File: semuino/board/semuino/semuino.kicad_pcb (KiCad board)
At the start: 2 copper layers, 95 x 95 mm, 63 parts, among them J1 12V_POWER_IN, J10 POW LED 3, J11 RF ON/OFF, J12 Screen, J13 Earth humidity sensor, J14 Select, J2 Select, J3 12V_POWER_OUT, J4 5V_POWER_IN, J5 RGB 1, J6 RGB 2, J7 RGB 3, J8 POW LED 1, J9 POW LED 2, Q1 2N2222A, Q2 P03P4L-04, Q3 2N2222A, Q4 2N2222A, Q5 2N2222A, Q6 P03P4L-04, Q7 P03P4L-04, Q8 P03P4L-04, U1 RtcArduino, U2 BPC_ESP8266-01_ESP-01, U3 BPC_DHT22, U4 BPC_Alim3_3V

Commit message: Après nettoyage et vérification des règles
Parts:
- removed ? (x3): , 
- moved R14 0.87 mm to (122.2, 58.5)
- moved J6 0.50 mm to (189.0, 111.0)
- moved J7 0.50 mm to (189.0, 100.0)
- moved Q3 0.50 mm to (130.5, 96.5)
- moved J4 0.46 mm to (177.0, 131.0)
- moved J5 0.46 mm to (189.0, 122.0)
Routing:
- net Net-(J6-Pin_2): track 43.0 -> 49.5 mm
- net Net-(Q8-S): track 18.4 -> 20.2 mm
- net SCL: track 119.2 -> 117.5 mm
- net Hum3: track 61.9 -> 60.4 mm
- net CmdP2: track 60.9 -> 59.6 mm
- net CmdP1: track 75.2 -> 74.1 mm
- net Net-(Q3-Pad2): track 11.7 -> 11.2 mm
- net Temp: track 65.5 -> 65.0 mm
- net Net-(Q6-G): track 29.7 -> 30.2 mm
- net Net-(J7-Pin_2): track 30.5 -> 31.0 mm
- net Net-(J7-Pin_1): track 6.00 -> 6.50 mm
- net Net-(J6-Pin_1): track 6.00 -> 6.50 mm

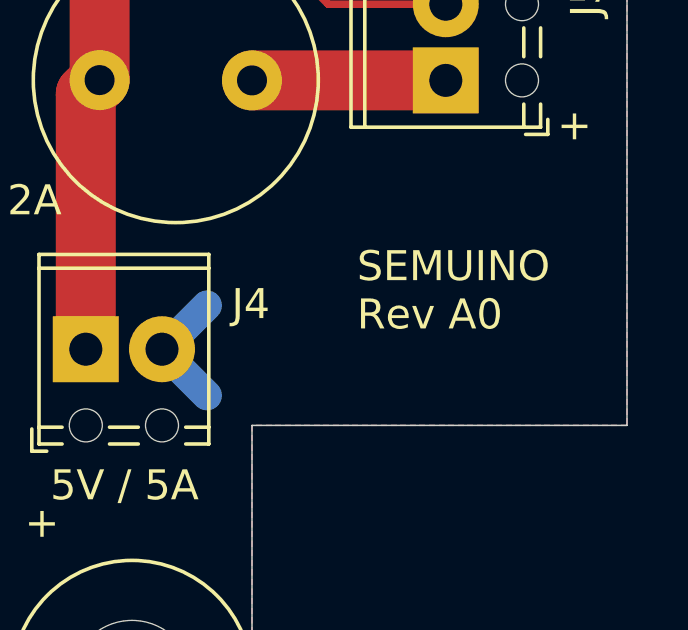
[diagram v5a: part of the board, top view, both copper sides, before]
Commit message: Modification valeur des résistances de commande + Marquage future A1
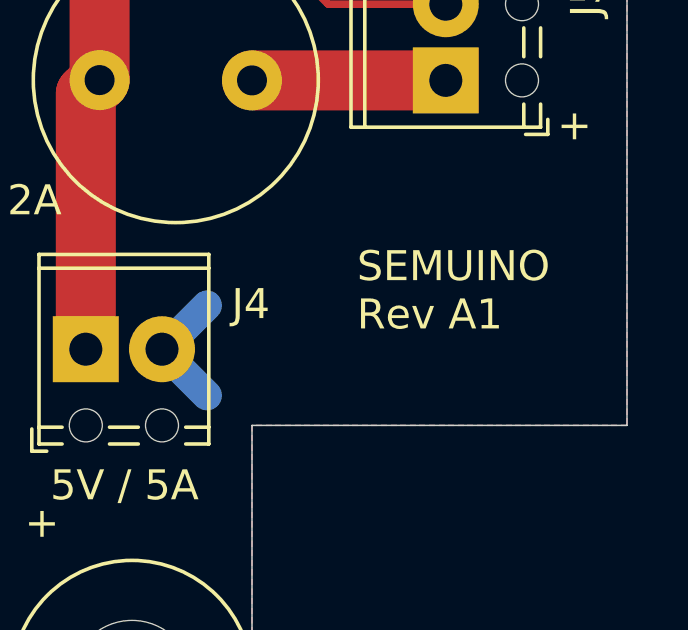
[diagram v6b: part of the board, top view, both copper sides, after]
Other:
- board text added: "SEMUINO Rev A1"
- board text removed: "SEMUINO Rev A0"
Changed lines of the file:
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@@
     (title "Semuino - Contrôleur de meuble à semis")
     (date "2023-09-21")
-    (rev "A0")
+    (rev "A1")
     (company "BPC")
     (comment 2 "Température ambiante - 3 Capteurs d'humidité")
@@
     (effects (font (size 1 1) (thickness 0.15)))
   )
-  (gr_text "SEMUINO\nRev A0" (at 186 129) (layer "F.SilkS")
+  (gr_text "SEMUINO\nRev A1" (at 186 129) (layer "F.SilkS")
     (effects (font (size 1 1) (thickness 0.15)) (justify left))
   )

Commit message: Passage carte semuino en A2 avec résistances 0R et commentaires/annotations suite mise en service de A0
Petit loupé niveau alim du nano qui doit se faire sur la broche 5V et non 3.3 (qui est une sortie)
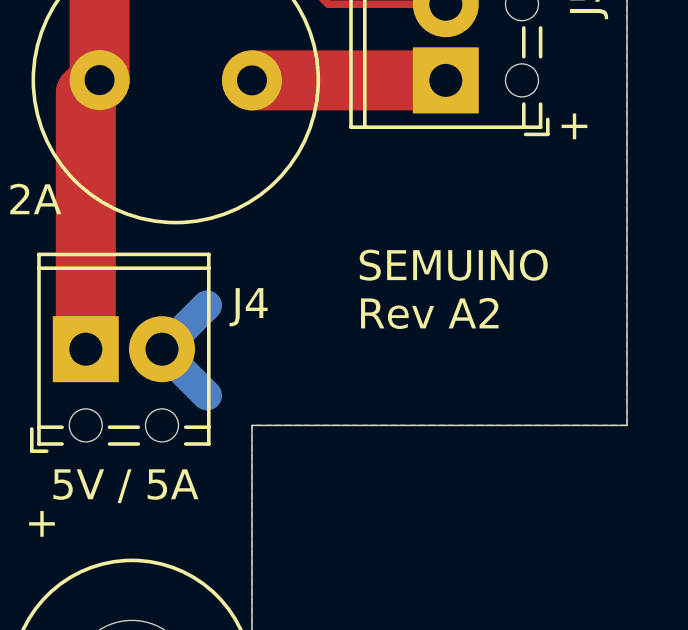
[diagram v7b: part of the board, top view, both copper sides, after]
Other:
- board text added: "SEMUINO Rev A2"
- board text removed: "SEMUINO Rev A1"
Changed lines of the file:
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@@
   (title_block
     (title "Semuino - Contrôleur de meuble à semis")
-    (date "2023-09-21")
-    (rev "A1")
+    (date "2023-12-22")
+    (rev "A2")
     (company "BPC")
     (comment 2 "Température ambiante - 3 Capteurs d'humidité")
@@
     (effects (font (size 1 1) (thickness 0.15)))
   )
-  (gr_text "SEMUINO\nRev A1" (at 186 129) (layer "F.SilkS")
+  (gr_text "SEMUINO\nRev A2" (at 186 129) (layer "F.SilkS")
     (effects (font (size 1 1) (thickness 0.15)) (justify left))
   )
